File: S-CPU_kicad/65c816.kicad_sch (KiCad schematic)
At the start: 4 parts, among them U1 65C816

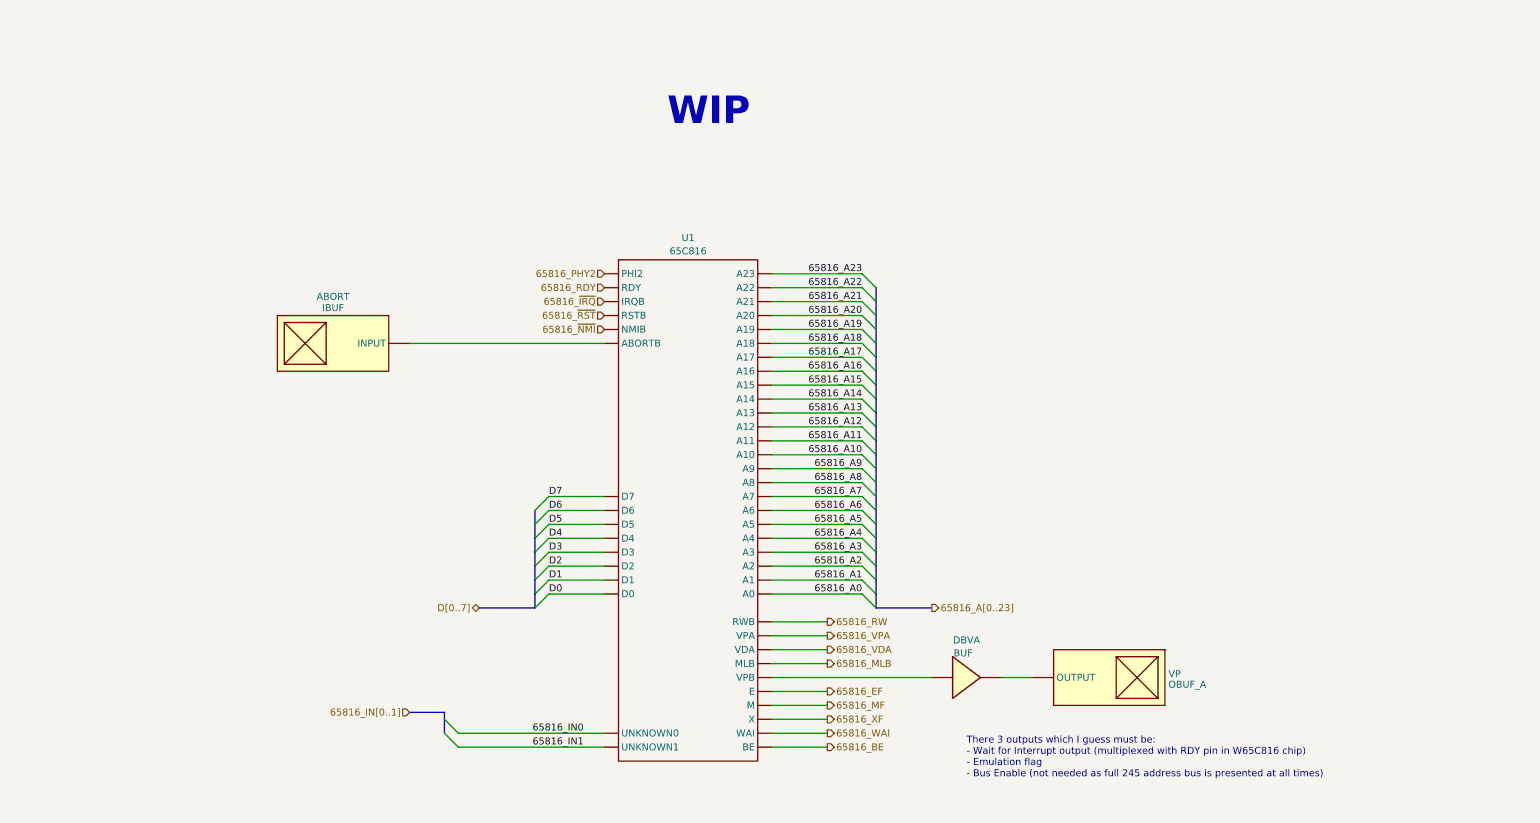
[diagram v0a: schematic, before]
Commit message: Big rework on the hierachical sheet to make thigs a bit clearer. PDF exported for Rev 0.1.
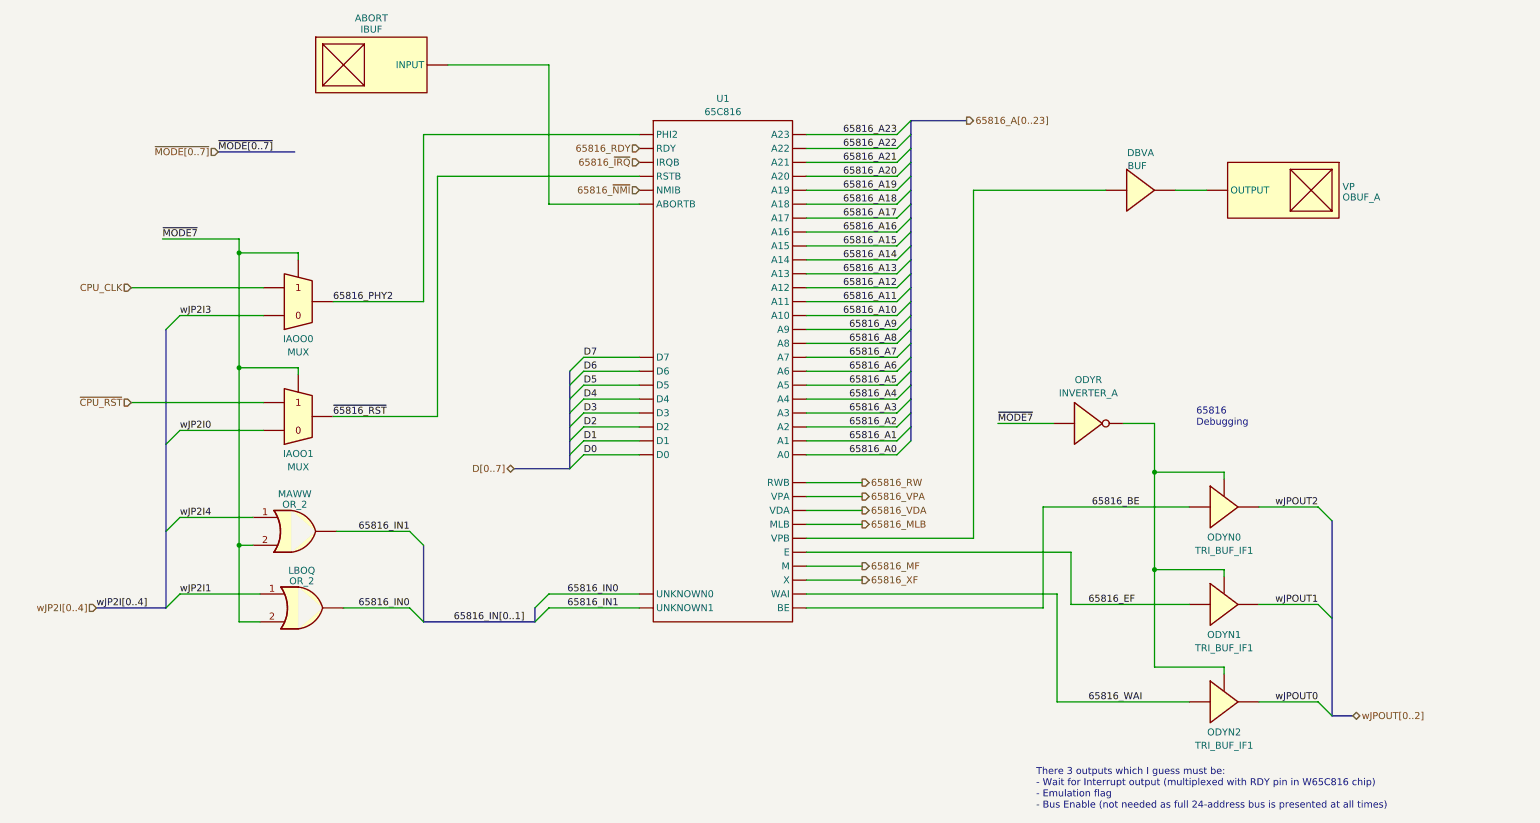
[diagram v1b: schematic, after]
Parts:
- added IAOO0, IAOO1: MUX, symbol Ricoh_Cells:MUX
- added LBOQ, MAWW: OR_2, symbol Ricoh_Cells:OR_2
- added ODYN0, ODYN1, ODYN2: TRI_BUF_IF1, symbol Ricoh_Cells:TRI_BUF_IF1
- added ODYR: INVERTER_A, symbol Ricoh_Cells:INVERTER_A
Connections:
- net 65816_BE: now also ODYN0.1 (IN), ODYN0.3 (IN)
- net 65816_EF: now also ODYN1.1 (IN), ODYN1.3 (IN)
- net 65816_IN0: now also LBOQ.3
- net 65816_IN1: now also MAWW.3
- net 65816_PHY2: now also IAOO0.4
- net 65816_WAI: now also ODYN2.1 (IN), ODYN2.3 (IN)
- net 65816_~{RST} renamed ~{65816_RST}
- net ~{65816_RST}: now also IAOO1.4
- new net: ODYN0.2 (~{ENA}), ODYN1.2 (~{ENA}), ODYN2.2 (~{ENA}), ODYR.2
- new net CPU_CLK: IAOO0.2
- new net wJP2I0: IAOO1.3
- new net wJP2I1: LBOQ.1
- new net wJP2I3: IAOO0.3
- new net wJP2I4: MAWW.1
- new net wJPOUT0: ODYN2.4
- new net wJPOUT1: ODYN1.4
- new net wJPOUT2: ODYN0.4
- new net ~{CPU_RST}: IAOO1.2
- new net ~{MODE7}: IAOO0.1, IAOO1.1, LBOQ.2, MAWW.2, ODYR.1
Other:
- note added: "65816 Debugging"
- note added: "There 3 outputs which I guess must be: - Wait for Interrupt output (multiplexed with RDY pin in W65C816 chip) - Emulation flag - Bus Enable (not needed as full 24-address bus is presented at all times)"
- note removed: "There 3 outputs which I guess must be: - Wait for Interrupt output (multiplexed with RDY pin in W65C816 chip) - Emulation flag - Bus Enable (not needed as full 245 address bus is presented at all times)"
- note removed: "WIP"
- company: (none) -> Author: Regis Galland
- title: (none) -> Reverse Engineered SNES S-CPU Schematics 
- moved on the sheet: ABORT, DBVA, U1, VP
